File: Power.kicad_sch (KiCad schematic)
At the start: 21 parts, among them U1 AP63205WU, U2 AP2112K-3.3, U4 TPS2116DRL

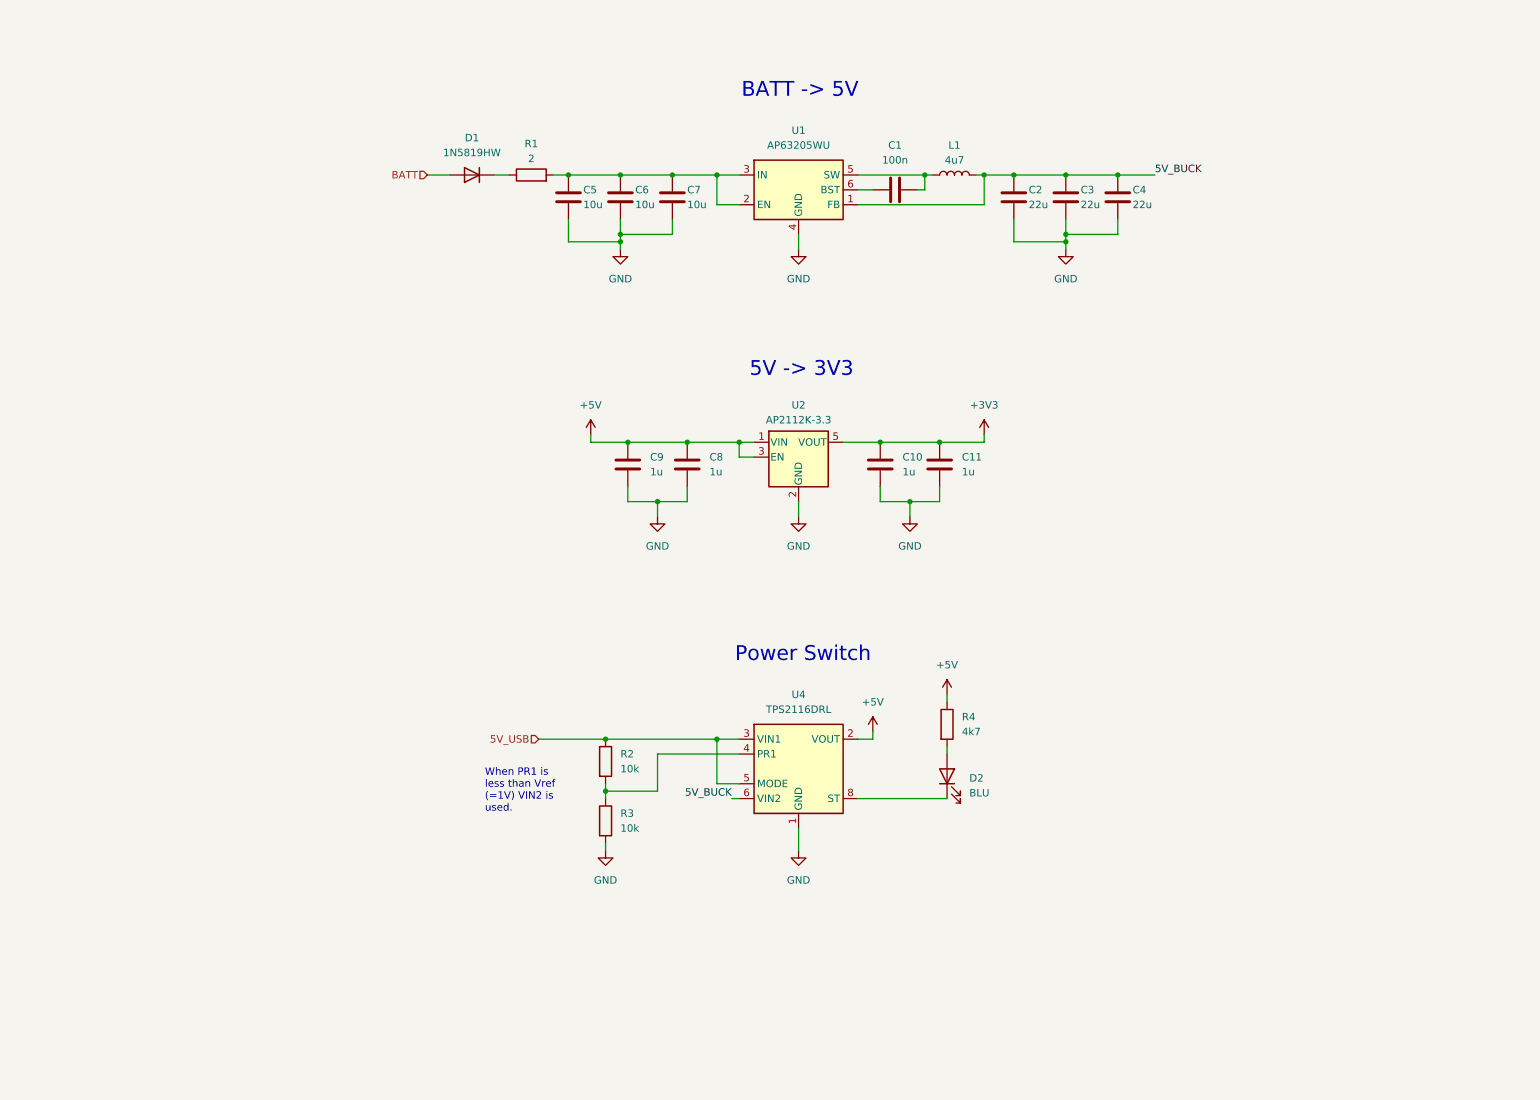
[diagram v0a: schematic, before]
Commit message: Added power schematic
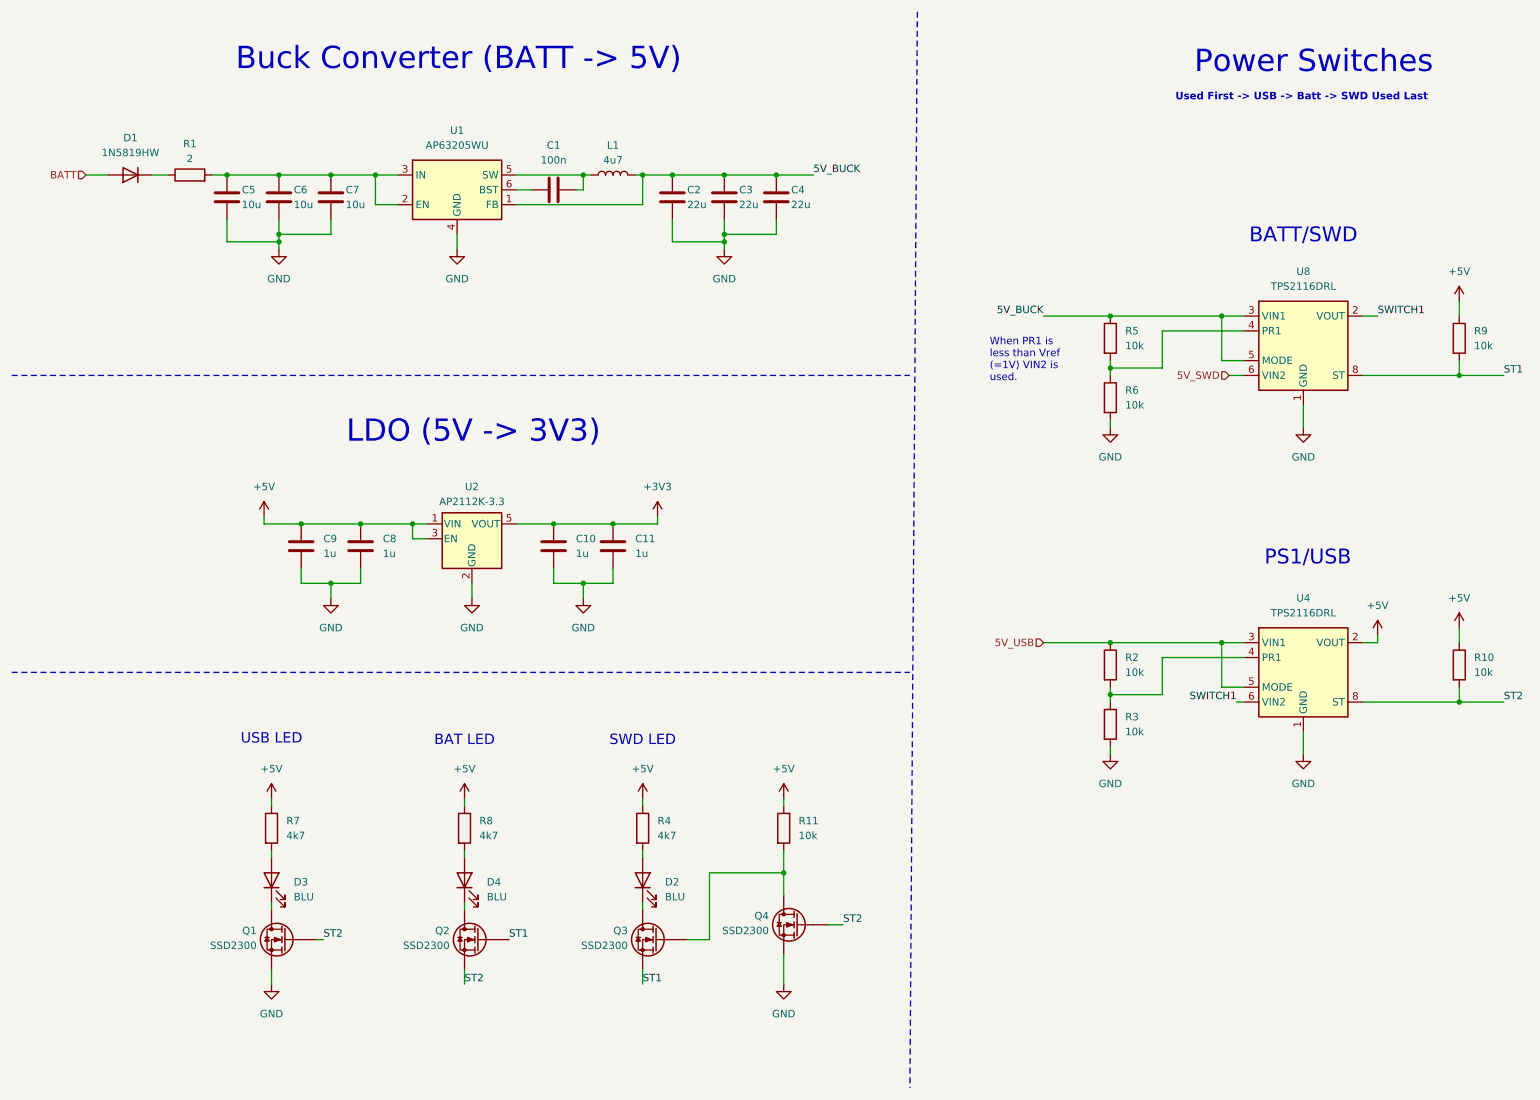
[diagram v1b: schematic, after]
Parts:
- added D3, D4: BLU, LED_SMD:LED_0603_1608Metric, symbol Device:LED
- added Q1, Q2, Q3, Q4: SSD2300, Button_Switch_SMD:SW_SPST_CK_KMS2xxGP, symbol Device:Q_NMOS
- added R10, R11, R5, R6, R9: 10k, Resistor_SMD:R_0603_1608Metric, symbol Device:R
- added R7, R8: 4k7, symbol Device:R
- added U8: TPS2116DRL, Package_TO_SOT_SMD:SOT-583-8, symbol Power_Management:TPS2116DRL
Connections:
- net +5V: now also R10.1, R11.1, R7.1, R8.1, R9.1
- net 5V_BUCK: now also R5.1, U8.3 (VIN1), U8.5 (MODE); no longer U4.6 (VIN2)
- net GND: now also Q1.S, Q4.S, R6.2, U8.1 (GND)
- net at D2.1 (K): now also Q3.D; no longer U4.8 (ST)
- new net: D4.1 (K), Q2.D
- new net: Q3.G, Q4.D, R11.2
- new net: D3.1 (K), Q1.D
- new net: R5.2, R6.1, U8.4 (PR1)
- new net: D3.2 (A), R7.2
- new net: D4.2 (A), R8.2
- new net 5V_SWD: U8.6 (VIN2)
- new net ST1: Q2.G, Q3.S, R9.2, U8.8 (ST)
- new net ST2: Q1.G, Q2.S, Q4.G, R10.2, U4.8 (ST)
- new net SWITCH1: U4.6 (VIN2), U8.2 (VOUT), U8.7 (VOUT)
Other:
- note added: "BAT LED"
- note added: "BATT/SWD"
- note added: "Buck Converter (BATT -> 5V)"
- note added: "LDO (5V -> 3V3)"
- note added: "PS1/USB"
- note added: "Power Switches"
- note added: "SWD LED"
- note added: "USB LED"
- note removed: "5V -> 3V3"
- note removed: "BATT -> 5V"
- note removed: "Power Switch"
- moved on the sheet: C1, C10, C11, C2, C3, C4, C5, C6, C7, C8, C9, D1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

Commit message: Added todos
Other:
- note added: "LED Indicators"
- moved on the sheet: D2, D3, D4, Q1, Q2, Q3, Q4, R11, R4, R7, R8
